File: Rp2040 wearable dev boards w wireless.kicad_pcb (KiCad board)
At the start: 4 copper layers, 40 x 65.7 mm, 80 parts, among them IC1 NRF24L01P-R7, J1 battery plug, J2 UJ31-CH-31-SMT-TR, J3 Conn_01x20, J4 Conn_01x20, J6 EMPCB.SMAFSTJ.B.HT, Q1 Si2301, SW1 B3U-1100P, SW2 power Switch, U1 MCP73831T-4ADI/OT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

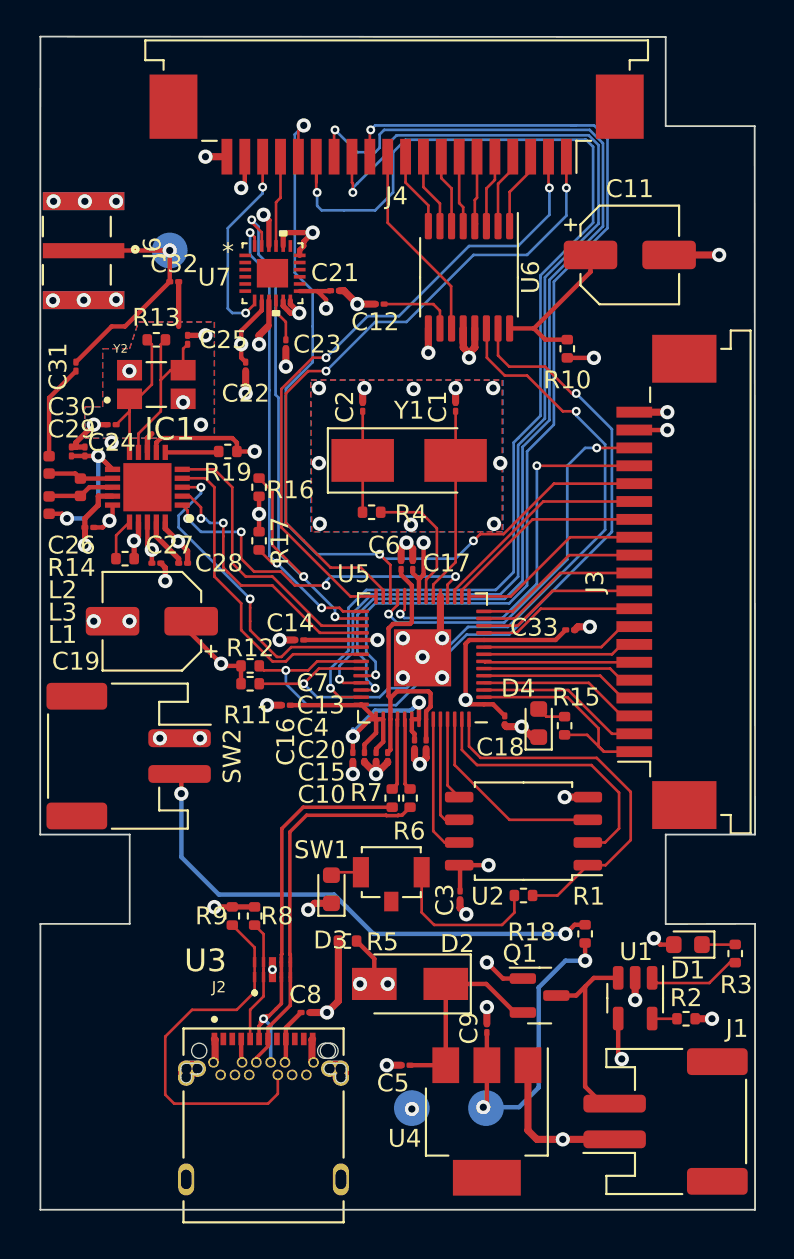
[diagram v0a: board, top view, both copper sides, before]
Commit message: finished cap bom, need to reroute part of it to fit cap sizes
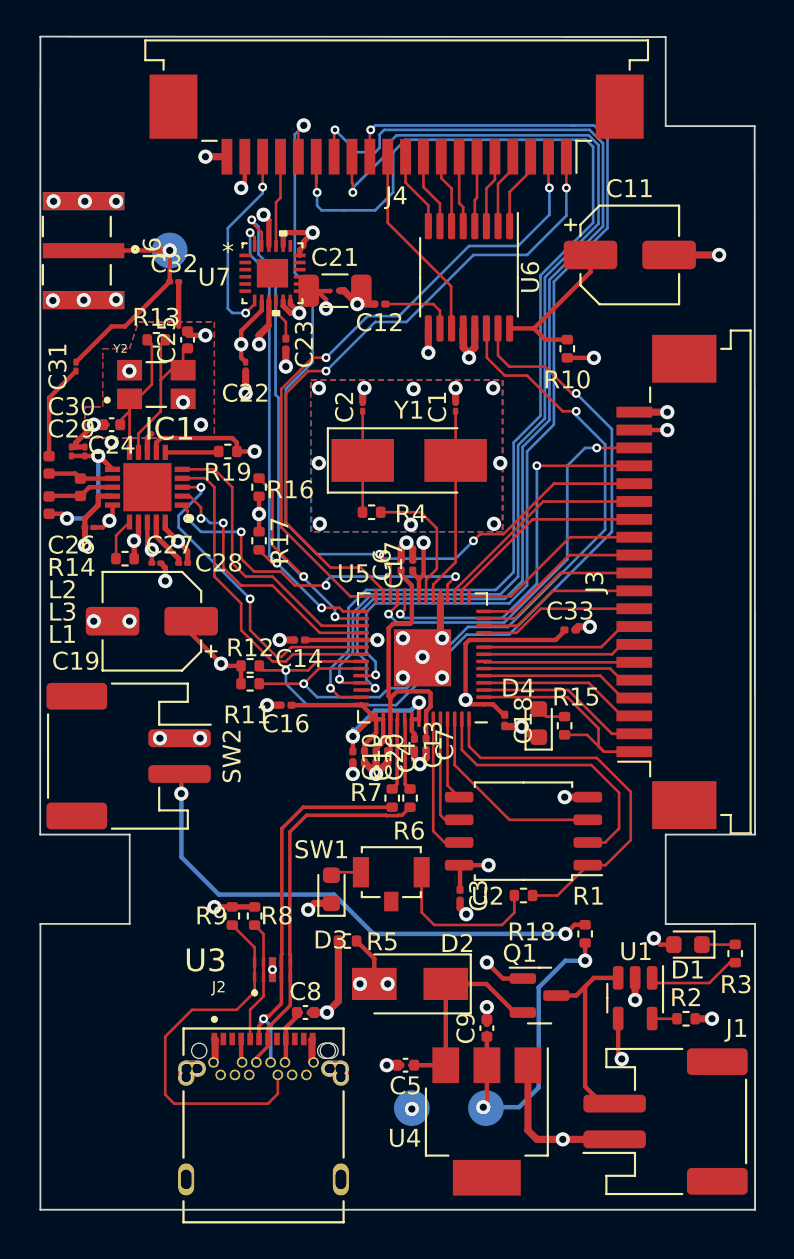
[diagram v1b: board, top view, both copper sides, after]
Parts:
- C10, C13, C14, C15, C16, C17, C18, C3, C33, C6, C7: value 100n -> 0.1u; footprint Capacitor_SMD:C_01005_0402Metric -> Capacitor_SMD:C_0201_0603Metric
- C12, C20, C23, C4: footprint Capacitor_SMD:C_01005_0402Metric -> Capacitor_SMD:C_0201_0603Metric
- C21: footprint Capacitor_SMD:C_01005_0402Metric -> Capacitor_SMD:C_1206_3216Metric
- C24, C25, C5, C8, C9: footprint Capacitor_SMD:C_01005_0402Metric -> Capacitor_SMD:C_0402_1005Metric
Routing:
- net GND: track 89.2 -> 86.9 mm, vias 65 -> 64
- net /Vmain: track 86.8 -> 89.1 mm, vias 18 -> 19

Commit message: more bom creation
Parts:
- removed TP2: ground test point, TestPoint:TestPoint_Pad_D2.0mm
- J2: value UJ31-CH-31-SMT-TR -> DX07S016JA1R1500; footprint usb-c footprint:CUI_UJ31-CH-31-SMT-TR -> usb-c:JAE_DX07S016JA1R1500
- moved J2 5.08 mm to (49.3, 95.4)
- moved C21 2.12 mm to (54.0, 47.0)
- moved C8 1.66 mm to (52.2, 88.0), turned to 90 degrees
- moved L2 0.25 mm to (36.8, 58.2)
- moved L3 0.25 mm to (36.8, 60.5)
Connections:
- J2 pad 1: (no net) -> GND
- J2 pad 2: (no net) -> /VBUS
- J2 pad 3: (no net) -> /CC1
- J2 pad 4: (no net) -> unconnected-(J2-Pad4)
- J2 pad 5: (no net) -> /USB-
- J2 pad 6: (no net) -> /USB+
- J2 pad S2: (no net) -> GND
- U3 pad 4: /USB- -> /USB+
- U3 pad 5: /USB+ -> /USB-
- U3 pad 6: /USB+ -> /USB-
- U3 pad 7: /USB- -> /USB+
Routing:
- net /VBUS: track 12.8 -> 23.6 mm, vias 5 -> 6
- net GND: track 86.9 -> 95.5 mm
- net /USB+: track 21.0 -> 25.9 mm
- net /USB-: track 22.4 -> 26.9 mm, vias 1 -> 0
- net /CC1: track 7.31 -> 11.3 mm
- net /Vmain: track 89.1 -> 86.6 mm, vias 19 -> 18
- net /CC2: track 21.3 -> 19.4 mm, vias 0 -> 2
